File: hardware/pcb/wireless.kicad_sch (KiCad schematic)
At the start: 1 part, among them IC2 MAYA-W386-00B

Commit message: contiunued working
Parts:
- IC2: MPN (none) -> MAYA-W383-00B; Manufacturer_Name u-blox -> (none); Manufacturer_Part_Number MAYA-W383-00B -> (none)
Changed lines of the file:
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@@
-			)
-		)
-		(property "Manufacturer_Name" "u-blox"
-			(at 184.15 613.03 0)
-			(hide yes)
-			(show_name no)
-			(do_not_autoplace no)
-			(effects
-				(font
-					(size 1.27 1.27)
-				)
-				(justify left top)
-			)
-		)
-		(property "Manufacturer_Part_Number" "MAYA-W383-00B"
-			(at 184.15 713.03 0)
-			(hide yes)
-			(show_name no)
-			(do_not_autoplace no)
-			(effects
-				(font
-					(size 1.27 1.27)
-				)
-				(justify left top)
-			)
-		)
-		(property "Mouser Part Number" ""
-			(at 184.15 813.03 0)
-			(hide yes)
-			(show_name no)
-			(do_not_autoplace no)
-			(effects
-				(font
-					(size 1.27 1.27)
-				)
-				(justify left top)
-			)
-		)
-		(property "Mouser Price/Stock" ""
-			(at 184.15 913.03 0)
-			(hide yes)
-			(show_name no)
-			(do_not_autoplace no)
-			(effects
-				(font
-					(size 1.27 1.27)
-				)
-				(justify left top)
 			)
 		)
@@
 			)
 		)
+		(property "MPN" "MAYA-W383-00B"
+			(at 132.08 118.11 0)
+			(hide yes)
+			(show_name no)
+			(do_not_autoplace no)
+			(effects
+				(font
+					(size 1.27 1.27)
+				)
+			)
+		)
+		(property "KLC_S3.3" ""
+			(at 132.08 118.11 0)
+			(hide yes)
+			(show_name no)
+			(do_not_autoplace no)
+			(effects
+				(font
+					(size 1.27 1.27)
+				)
+			)
+		)
+		(property "KLC_S4.1" ""
+			(at 132.08 118.11 0)
+			(hide yes)
+			(show_name no)
+			(do_not_autoplace no)
+			(effects
+				(font
+					(size 1.27 1.27)
+				)
+			)
+		)

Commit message: bunch of small changes
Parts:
- added C30, C31: 9p, symbol Device:C_Small
- added Y3: 32kHz768, Crystal:Crystal_SMD_MicroCrystal_CC7V-T1A-2Pin_3.2x1.5mm, symbol Device:Crystal
- IC2: Manufacturer_Name (none) -> u-blox; Manufacturer_Part_Number (none) -> MAYA-W383-00B
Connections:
- net GND: now also C30.2, C31.2
- net at IC2.C2 (SLP_XTAL_IN): now also C31.1, Y3.1
- net at IC2.D2 (SLP_XTAL_OUT): now also C30.1, Y3.2

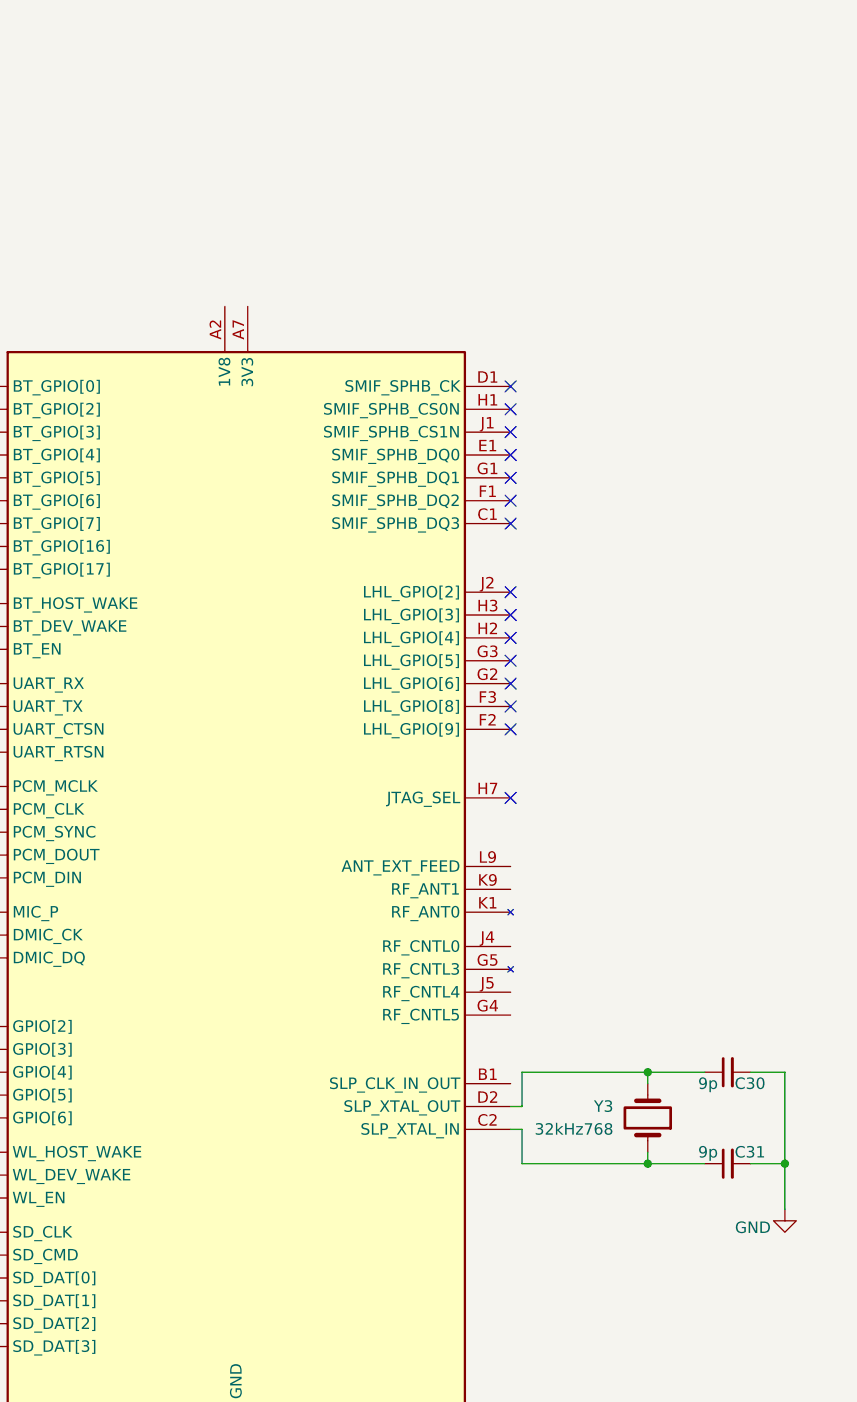
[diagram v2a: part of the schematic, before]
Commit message: bunch of small audio changes
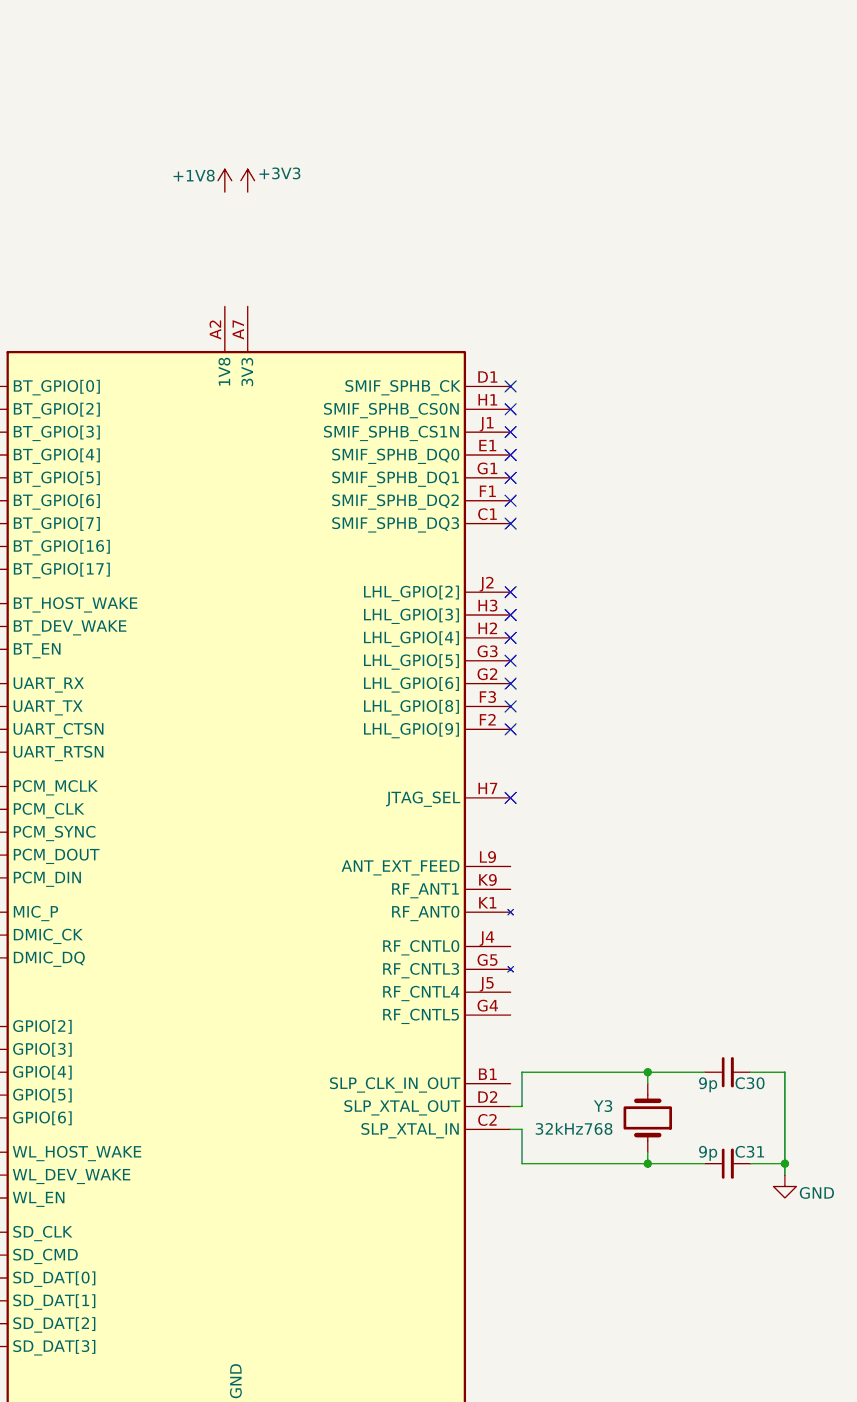
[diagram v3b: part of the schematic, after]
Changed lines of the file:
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@@
 	(paper "A4")
+	(junction
+		(at 193.04 149.86)
+		(diameter 0)
+		(color 0 0 0 0)
+	)
 	(junction
 		(at 177.8 139.7)
@@
 	)
 	(junction
-		(at 193.04 149.86)
-		(diameter 0)
-		(color 0 0 0 0)
-	)
-	(junction
 		(at 177.8 149.86)
 		(diameter 0)
@@
 	(wire
 		(pts
-			(xy 193.04 154.94) (xy 193.04 149.86)
+			(xy 193.04 151.13) (xy 193.04 149.86)
 		)
 		(stroke
@@
 	)
 	(symbol
+		(lib_id "power:+3V3")
+		(at 133.35 41.91 0)
+		(unit 1)
+		(body_style 1)
+		(exclude_from_sim no)
+		(in_bom yes)
+		(on_board yes)
+		(in_pos_files yes)
+		(dnp no)
+		(property "Reference" "#PWR0102"
+			(at 133.35 45.72 0)
+			(hide yes)
+			(show_name no)
+			(do_not_autoplace no)
+			(effects
+				(font
+					(size 1.27 1.27)
+				)
+			)
+		)
+		(property "Value" "+3V3"
+			(at 136.906 39.878 0)
+			(show_name no)
+			(do_not_autoplace no)
+			(effects
+				(font
+					(size 1.27 1.27)
+				)
+			)
+		)
+		(property "Footprint" ""
+			(at 133.35 41.91 0)
+			(hide yes)
+			(show_name no)
+			(do_not_autoplace no)
+			(effects
+				(font
+					(size 1.27 1.27)
+				)
+			)
+		)
+		(property "Datasheet" ""
+			(at 133.35 41.91 0)
+			(hide yes)
+			(show_name no)
+			(do_not_autoplace no)
+			(effects
+				(font
+					(size 1.27 1.27)
+				)
+			)
+		)
+		(property "Description" "Power symbol creates a global label with name \"+3V3\""
+			(at 133.35 41.91 0)
+			(hide yes)
+			(show_name no)
+			(do_not_autoplace no)
+			(effects
+				(font
+					(size 1.27 1.27)
+				)
+			)
+		)
+		(pin "1"
+		)
+		(instances
+			(project "meko"
+				(path "/da54f10a-146b-4941-a9c7-55c7173bb101/cf3a540d-b7d8-4416-baa0-bfc874a83584"
+					(reference "#PWR0102")
+					(unit 1)
+				)
+			)
+		)
+	)
+	(symbol
+		(lib_id "power:VDD")
+		(at 130.81 41.91 0)
+		(mirror y)
+		(unit 1)
+		(body_style 1)
+		(exclude_from_sim no)
+		(in_bom yes)
+		(on_board yes)
+		(in_pos_files yes)
+		(dnp no)
+		(property "Reference" "#PWR0103"
+			(at 130.81 45.72 0)
+			(hide yes)
+			(show_name no)
+			(do_not_autoplace no)
+			(effects
+				(font
+					(size 1.27 1.27)
+				)
+			)
+		)
+		(property "Value" "+1V8"
+			(at 129.794 40.132 0)
+			(show_name no)
+			(do_not_autoplace no)
+			(effects
+				(font
+					(size 1.27 1.27)
+				)
+				(justify left)
+			)
+		)
+		(property "Footprint" ""
+			(at 130.81 41.91 0)
+			(hide yes)
+			(show_name no)
+			(do_not_autoplace no)
+			(effects
+				(font
+					(size 1.27 1.27)
+				)
+			)
+		)
+		(property "Datasheet" ""
+			(at 130.81 41.91 0)
+			(hide yes)
+			(show_name no)
+			(do_not_autoplace no)
+			(effects
+				(font
+					(size 1.27 1.27)
+				)
+			)
+		)
+		(property "Description" "Power symbol creates a global label with name \"VDD\""
+			(at 130.81 41.91 0)
+			(hide yes)
+			(show_name no)
+			(do_not_autoplace no)
+			(effects
+				(font
+					(size 1.27 1.27)
+				)
+			)
+		)
+		(pin "1"
+		)
+		(instances
+			(project "meko"
+				(path "/da54f10a-146b-4941-a9c7-55c7173bb101/cf3a540d-b7d8-4416-baa0-bfc874a83584"
+					(reference "#PWR0103")
+					(unit 1)
+				)
+			)
+		)
+	)
+	(symbol
 		(lib_id "Device:C_Small")
 		(at 186.69 149.86 90)
@@
 	(symbol
 		(lib_id "power:GND")
-		(at 193.04 154.94 0)
-		(mirror y)
+		(at 193.04 151.13 0)
 		(unit 1)
 		(body_style 1)
@@
 		(dnp no)
 		(property "Reference" "#PWR069"
-			(at 193.04 161.29 0)
+			(at 193.04 157.48 0)
 			(hide yes)
 			(show_name no)
@@
 		)
 		(property "Value" "GND"
-			(at 189.484 156.972 0)
+			(at 196.596 153.162 0)
 			(show_name no)
 			(do_not_autoplace no)
@@
 		)
 		(property "Footprint" ""
-			(at 193.04 154.94 0)
+			(at 193.04 151.13 0)
 			(hide yes)
 			(show_name no)
@@
 		)
 		(property "Datasheet" ""
-			(at 193.04 154.94 0)
+			(at 193.04 151.13 0)
 			(hide yes)
 			(show_name no)
@@
 		)
 		(property "Description" "Power symbol creates a global label with name \"GND\" , ground"
-			(at 193.04 154.94 0)
-			(hide yes)
-			(show_name no)
+			(at 193.04 151.13 0)
+			(hide yes)
+			(show_name no)

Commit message: bunch of small audio and rf changes
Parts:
- added C39, C42: 1u, symbol Device:C_Small
- added R29, R30, R31, R32, R33: 47k, symbol Device:R_Small
- added R34, R35, R38, R39: 10k, symbol Device:R_Small
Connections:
- net 3V3 is gone; now on net +3V3: IC2.A7 (3V3), IC2.B7 (3V3)
- net +1V8: now also IC2.A2 (1V8), C42.2
- net +3V3: now also C39.1, R29.1, R30.1, R31.1, R32.1, R33.1
- net GND: now also IC2.H7 (JTAG_SEL), C39.2, C42.1, R34.1, R35.1, R38.1, R39.1
- net DAT1: now reaches IC2.A3 (SD_DAT[1])
- net DAT1: now also R31.2
- net CK: now reaches IC2.A4 (SD_CLK)
- net DAT3: now reaches IC2.A5 (SD_DAT[3])
- net DAT3: now also R33.2
- net DAT0: now reaches IC2.B3 (SD_DAT[0])
- net DAT0: now also R30.2
- net CMD: now reaches IC2.B4 (SD_CMD)
- net CMD: now also R29.2
- net DAT2: now reaches IC2.B5 (SD_DAT[2])
- net DAT2: now also R32.2
- net BCLK: now reaches IC2.D8 (PCM_CLK)
- net BT.HOST_WAKE: now reaches IC2.E7 (BT_HOST_WAKE)
- net BT.HOST_WAKE: now also R39.2
- net MCLK: now reaches IC2.E8 (PCM_MCLK)
- net DIN: now reaches IC2.E9 (PCM_DIN)
- net WL.HOST_WAKE: now reaches IC2.F7 (WL_HOST_WAKE)
- net WL.HOST_WAKE: now also R34.2
- net FSYNC: now reaches IC2.F8 (PCM_SYNC)
- net DOUT: now reaches IC2.F9 (PCM_DOUT)
- net RX: now reaches IC2.G8 (UART_RX)
- net TX: now reaches IC2.G9 (UART_TX)
- net CTSN: now reaches IC2.H8 (UART_CTSN)
- net RTSN: now reaches IC2.H9 (UART_RTSN)
- net WL.EN: now reaches IC2.J3 (WL_EN)
- net BT.EN: now reaches IC2.J7 (BT_EN)
- net WL.DEV_WAKE: now reaches IC2.J8 (WL_DEV_WAKE)
- net WL.DEV_WAKE: now also R35.2
- net BT.DEV_WAKE: now reaches IC2.J9 (BT_DEV_WAKE)
- net BT.DEV_WAKE: now also R38.2
- net at IC2.K9 (RF_ANT1): now also IC2.L9 (ANT_EXT_FEED)
- no-connect marks 15 -> 35
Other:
- note added: "BT EN has internal pull down"
- note added: "External Memory/Flash"
- note added: "JTAG Pins"
- note added: "Mic input, and digital outputs"
- note added: "RF Switch Control Lines"
- note added: "WL EN has internal pull down"
- moved on the sheet: C30, C31, IC2, Y3

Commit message: looking over stuff, added caps
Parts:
- C30, C31, C39, C42: footprint (none) -> Capacitor_SMD:C_0402_1005Metric
- R29, R30, R31, R32, R33, R34, R35, R38, R39: footprint (none) -> Resistor_SMD:R_0402_1005Metric
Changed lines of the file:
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@@
 			)
 		)
-		(property "Footprint" ""
+		(property "Footprint" "Capacitor_SMD:C_0402_1005Metric"
 			(at 147.32 34.29 0)
 			(hide yes)
@@
 			)
 		)
-		(property "Footprint" ""
+		(property "Footprint" "Capacitor_SMD:C_0402_1005Metric"
 			(at 162.56 34.29 0)
 			(hide yes)
@@
 			)
 		)
-		(property "Footprint" ""
+		(property "Footprint" "Resistor_SMD:R_0402_1005Metric"
 			(at 76.2 133.35 0)
 			(hide yes)
@@
 			)
 		)
-		(property "Footprint" ""
+		(property "Footprint" "Resistor_SMD:R_0402_1005Metric"
 			(at 69.85 133.35 0)
 			(hide yes)
@@
 			)
 		)
-		(property "Footprint" ""
+		(property "Footprint" "Capacitor_SMD:C_0402_1005Metric"
 			(at 209.55 130.81 0)
 			(hide yes)
@@
 			)
 		)
-		(property "Footprint" ""
+		(property "Footprint" "Resistor_SMD:R_0402_1005Metric"
 			(at 63.5 133.35 0)
 			(hide yes)
@@
 			)
 		)
-		(property "Footprint" ""
+		(property "Footprint" "Resistor_SMD:R_0402_1005Metric"
 			(at 90.17 78.74 0)
 			(hide yes)
@@
 			)
 		)
-		(property "Footprint" ""
+		(property "Footprint" "Capacitor_SMD:C_0402_1005Metric"
 			(at 209.55 120.65 0)
 			(hide yes)
@@
 			)
 		)
-		(property "Footprint" ""
+		(property "Footprint" "Resistor_SMD:R_0402_1005Metric"
 			(at 121.92 160.02 0)
 			(hide yes)
@@
 			)
 		)
-		(property "Footprint" ""
+		(property "Footprint" "Resistor_SMD:R_0402_1005Metric"
 			(at 96.52 78.74 0)
 			(hide yes)
@@
 			)
 		)
-		(property "Footprint" ""
+		(property "Footprint" "Resistor_SMD:R_0402_1005Metric"
 			(at 57.15 133.35 0)
 			(hide yes)
@@
 			)
 		)
-		(property "Footprint" ""
+		(property "Footprint" "Resistor_SMD:R_0402_1005Metric"
 			(at 115.57 160.02 0)
 			(hide yes)
@@
 			)
 		)
-		(property "Footprint" ""
+		(property "Footprint" "Resistor_SMD:R_0402_1005Metric"
 			(at 82.55 133.35 0)
 			(hide yes)

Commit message: started cleaning up schematic
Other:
- company: (none) -> Gensis
- title: (none) -> Wireless
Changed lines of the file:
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@@
 	(generator_version "10.0")
 	(paper "A4")
+	(title_block
+		(title "Wireless")
+		(rev "v1.0.0")
+		(company "Gensis")
+	)
 	(text "WL EN has internal pull down"
 		(exclude_from_sim no)

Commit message: main board: fixed schematic errors, made sama7 symbol better
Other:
- note added: "Connecting the output to the integrated PCB antenna"
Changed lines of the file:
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@@
+		)
+	)
+	(text "Connecting the output to the integrated PCB antenna"
+		(exclude_from_sim no)
+		(at 187.452 99.314 0)
+		(effects
+			(font
+				(size 1.27 1.27)
+			)
+			(justify left)
 		)
 	)
